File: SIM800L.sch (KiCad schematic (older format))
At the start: 7 parts

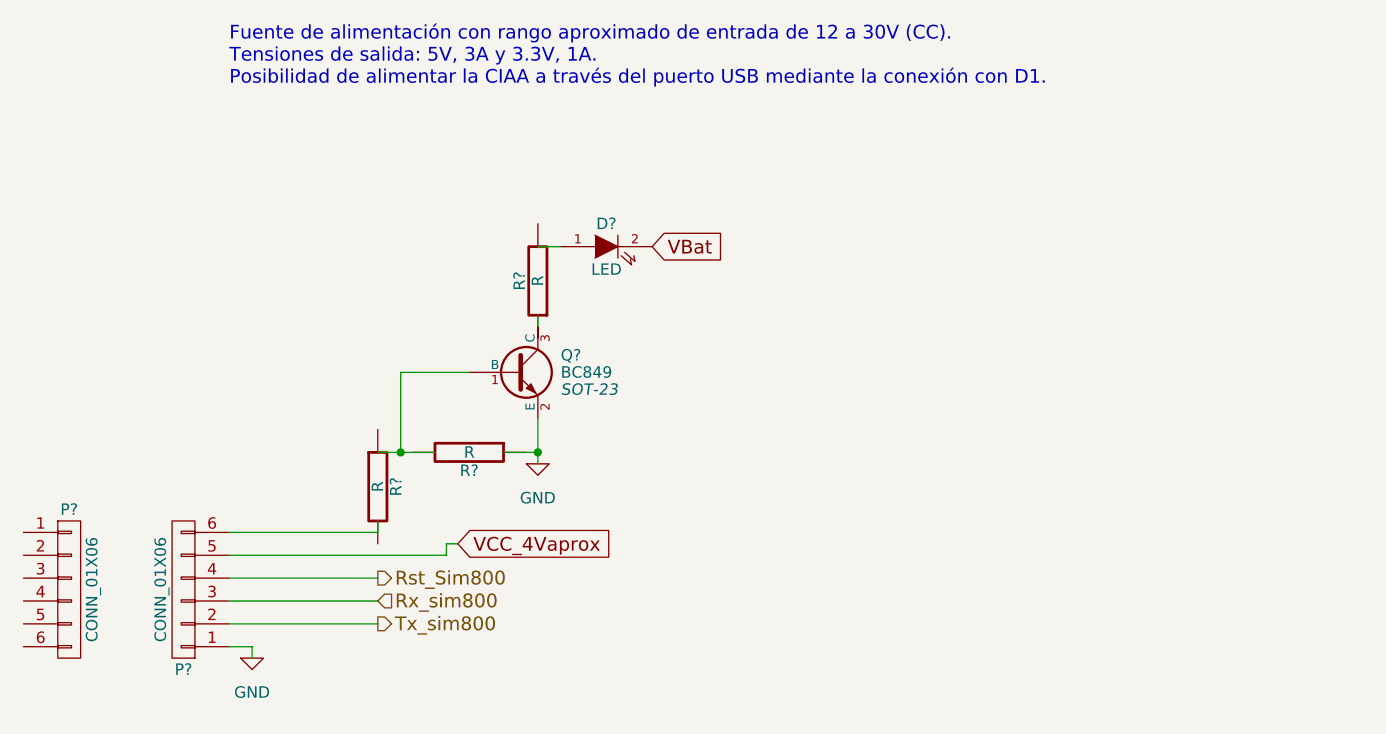
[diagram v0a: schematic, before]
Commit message: Max3232 -ok, Fuente ok, Buttons y Leds, OK. Fuente correinte OK, Falta Potenciometros y LM35.
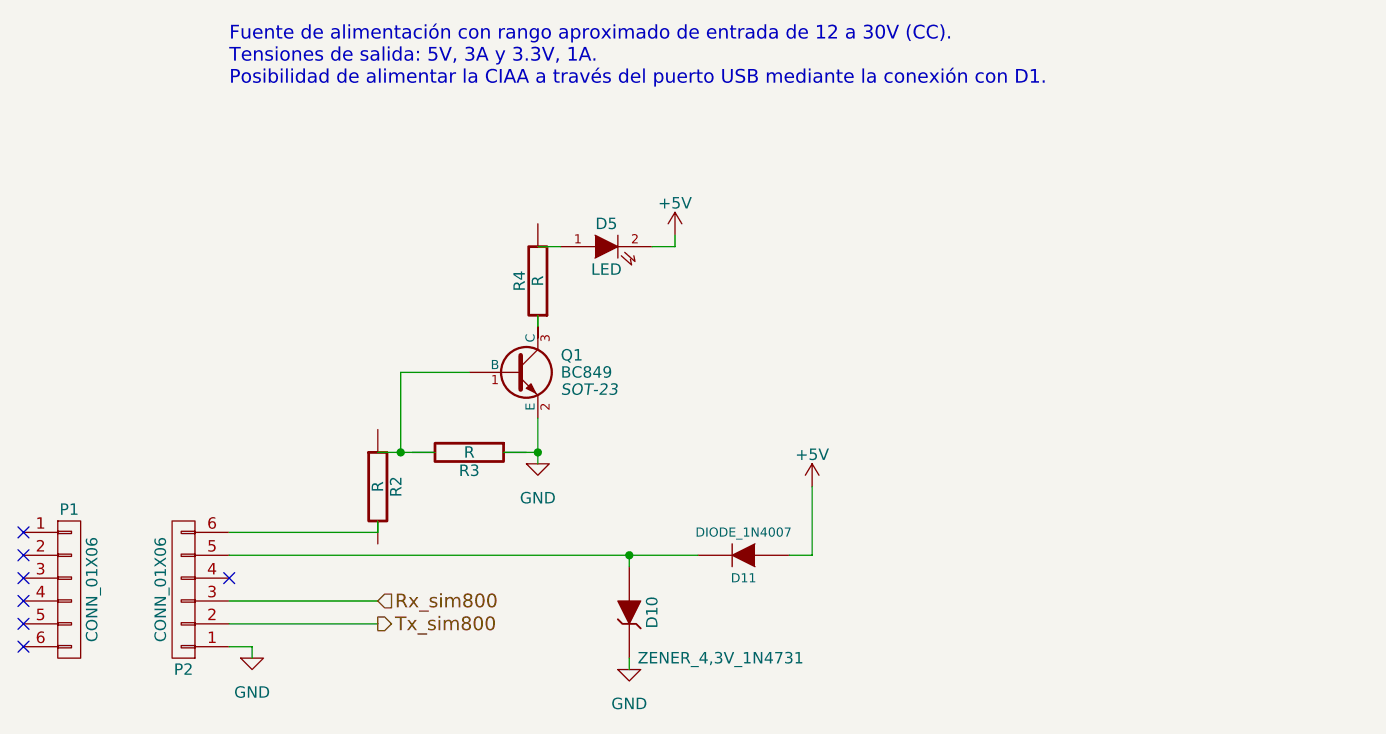
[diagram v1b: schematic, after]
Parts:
- added D10: ZENER_4,3V_1N4731, symbol ZENER
- added D11: DIODE_1N4007, symbol DIODE
- gave numbers to parts that had none: 7
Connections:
- net labels added: +5V
- net labels removed: Rst_Sim800, VBat, VCC_4Vaprox
- wire segments 17 -> 20
- no-connect marks 0 -> 7
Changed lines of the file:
@@
 $Descr A4 11693 8268
 encoding utf-8
-Sheet 4 4
+Sheet 4 6
 Title "CIAA Fuente de alimentación"
 Date "11 may 2015"
@@
 Fuente de alimentación con rango aproximado de entrada de 12 a 30V (CC).\nTensiones de salida: 5V, 3A y 3.3V, 1A.\nPosibilidad de alimentar la CIAA a través del puerto USB mediante la conexión con D1.
 $Comp
-L CONN_01X06 P?
+L CONN_01X06 P1
 U 1 1 5819E820
 P 3350 3450
-F 0 "P?" H 3350 3800 50  0000 C CNN
+F 0 "P1" H 3350 3800 50  0000 C CNN
 F 1 "CONN_01X06" V 3450 3450 50  0000 C CNN
 F 2 "" H 3350 3450 50  0000 C CNN
@@
 $EndComp
 $Comp
-L CONN_01X06 P?
+L CONN_01X06 P2
 U 1 1 5819E8C4
 P 3850 3450
-F 0 "P?" H 3850 3800 50  0000 C CNN
+F 0 "P2" H 3850 3800 50  0000 C CNN
 F 1 "CONN_01X06" V 3950 3450 50  0000 C CNN
 F 2 "" H 3850 3450 50  0000 C CNN
@@
 $EndComp
 $Comp
-L GND #PWR?
+L GND #PWR029
 U 1 1 5819E9A3
 P 4150 3750
-F 0 "#PWR?" H 4150 3500 50  0001 C CNN
+F 0 "#PWR029" H 4150 3500 50  0001 C CNN
 F 1 "GND" H 4150 3600 50  0000 C CNN
 F 2 "" H 4150 3750 50  0000 C CNN
@@
 	4050 3500 4700 3500
 Wire Wire Line
-	4050 3400 4700 3400
-Wire Wire Line
-	4050 3300 5000 3300
+	4050 3300 6100 3300
 Wire Wire Line
 	4050 3200 4700 3200
@@
 Text HLabel 4700 3600 2    60   Output ~ 0
 Tx_sim800
-Text HLabel 4700 3400 2    60   Output ~ 0
-Rst_Sim800
-$Comp
-L R R?
+$Comp
+L R R2
 U 1 1 5819EB4E
 P 4700 3000
-F 0 "R?" V 4780 3000 50  0000 C CNN
+F 0 "R2" V 4780 3000 50  0000 C CNN
 F 1 "R" V 4700 3000 50  0000 C CNN
 F 2 "" V 4630 3000 50  0000 C CNN
@@
 $EndComp
 $Comp
-L R R?
+L R R3
 U 1 1 5819EB9D
 P 5100 2850
-F 0 "R?" V 5180 2850 50  0000 C CNN
+F 0 "R3" V 5180 2850 50  0000 C CNN
 F 1 "R" V 5100 2850 50  0000 C CNN
 F 2 "" V 5030 2850 50  0000 C CNN
@@
 $EndComp
 $Comp
-L BC849 Q?
+L BC849 Q1
 U 1 1 5819ECA4
 P 5300 2500
-F 0 "Q?" H 5500 2575 50  0000 L CNN
+F 0 "Q1" H 5500 2575 50  0000 L CNN
 F 1 "BC849" H 5500 2500 50  0000 L CNN
 F 2 "SOT-23" H 5500 2425 50  0000 L CIN
@@
 $EndComp
 $Comp
-L GND #PWR?
+L GND #PWR030
 U 1 1 5819EDBF
 P 5400 2900
-F 0 "#PWR?" H 5400 2650 50  0001 C CNN
+F 0 "#PWR030" H 5400 2650 50  0001 C CNN
 F 1 "GND" H 5400 2750 50  0000 C CNN
 F 2 "" H 5400 2900 50  0000 C CNN
@@
 Connection ~ 4800 2850
 $Comp
-L R R?
+L R R4
 U 1 1 5819EF54
 P 5400 2100
-F 0 "R?" V 5480 2100 50  0000 C CNN
+F 0 "R4" V 5480 2100 50  0000 C CNN
 F 1 "R" V 5400 2100 50  0000 C CNN
 F 2 "" V 5330 2100 50  0000 C CNN
@@
 $EndComp
 $Comp
-L LED D?
+L LED D5
 U 1 1 5819EFAC
 P 5700 1950
-F 0 "D?" H 5700 2050 50  0000 C CNN
+F 0 "D5" H 5700 2050 50  0000 C CNN
 F 1 "LED" H 5700 1850 50  0000 C CNN
 F 2 "" H 5700 1950 50  0000 C CNN
@@
 Wire Wire Line
 	5400 2250 5400 2300
-Text GLabel 5050 3250 2    60   Input ~ 0
-VCC_4Vaprox
-Wire Wire Line
-	5050 3250 5000 3250
-Wire Wire Line
-	5000 3250 5000 3300
-Text GLabel 5900 1950 2    60   Input ~ 0
-VBat
+NoConn ~ 3150 3700
+NoConn ~ 3150 3600
+NoConn ~ 3150 3500
+NoConn ~ 3150 3400
+NoConn ~ 3150 3300
+NoConn ~ 3150 3200
+$Comp
+L +5V #PWR031
+U 1 1 5819C8CC
+P 6000 1900
+F 0 "#PWR031" H 6000 1750 50  0001 C CNN
+F 1 "+5V" H 6000 2040 50  0000 C CNN
+F 2 "" H 6000 1900 50  0000 C CNN
+F 3 "" H 6000 1900 50  0000 C CNN
+	1    6000 1900
+	1    0    0    -1
+$EndComp
+Wire Wire Line
+	5900 1950 6000 1950
+Wire Wire Line
+	6000 1950 6000 1900
+$Comp
+L ZENER D10
+U 1 1 5819CB42
+P 5800 3550
+F 0 "D10" H 5800 3650 50  0000 C CNN
+F 1 "ZENER_4,3V_1N4731" V 6000 3950 50  0000 C CNN
+F 2 "" H 5800 3550 50  0000 C CNN
+F 3 "" H 5800 3550 50  0000 C CNN
+	1    5800 3550
+	0    1    1    0
+$EndComp
+Wire Wire Line
+	5800 3300 5800 3350
+$Comp
+L GND #PWR032
+U 1 1 5819CBD8
+P 5800 3800
+F 0 "#PWR032" H 5800 3550 50  0001 C CNN
+F 1 "GND" H 5800 3650 50  0000 C CNN
+F 2 "" H 5800 3800 50  0000 C CNN
+F 3 "" H 5800 3800 50  0000 C CNN
+	1    5800 3800
+	1    0    0    -1
+$EndComp
+Wire Wire Line
+	5800 3750 5800 3800
+$Comp
+L DIODE D11
+U 1 1 5819CC13
+P 6300 3300
+F 0 "D11" H 6300 3400 40  0000 C CNN
+F 1 "DIODE_1N4007" H 6300 3200 40  0000 C CNN
+F 2 "" H 6300 3300 60  0000 C CNN
+F 3 "" H 6300 3300 60  0000 C CNN
+	1    6300 3300
+	-1   0    0    1
+$EndComp
+$Comp
+L +5V #PWR033
+U 1 1 5819CCE8
+P 6600 3000
+F 0 "#PWR033" H 6600 2850 50  0001 C CNN
+F 1 "+5V" H 6600 3140 50  0000 C CNN
+F 2 "" H 6600 3000 50  0000 C CNN
+F 3 "" H 6600 3000 50  0000 C CNN
+	1    6600 3000
+	1    0    0    -1
+$EndComp
+Wire Wire Line
+	6600 3000 6600 3300
+Wire Wire Line
+	6600 3300 6500 3300
+Connection ~ 5800 3300
+NoConn ~ 4050 3400
 $EndSCHEMATC

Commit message: Arreglo Max3232_ok, Fuente_ok, Buttons&Leds, OK.Fuente correinte OK, Potenciometros OK y LM35 OK.
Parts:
- removed P1: CONN_01X06, symbol CONN_01X06
- added P3: CONN_01X06, symbol CONN_01X06
- renumbered D10 to D6, D11 to D7, P2 to P4
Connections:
- wire segments 20 -> 21
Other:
- moved on the sheet: D5, Q1, R2, R3, R4
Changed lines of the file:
@@
 EESchema Schematic File Version 2
-LIBS:ciaa-nxp-rescue
-LIBS:power
-LIBS:device
-LIBS:transistors
-LIBS:conn
-LIBS:linear
-LIBS:regul
-LIBS:74xx
-LIBS:cmos4000
-LIBS:adc-dac
-LIBS:memory
-LIBS:xilinx
-LIBS:microcontrollers
-LIBS:dsp
-LIBS:microchip
-LIBS:analog_switches
-LIBS:motorola
-LIBS:texas
-LIBS:intel
-LIBS:audio
-LIBS:interface
-LIBS:digital-audio
-LIBS:philips
-LIBS:display
-LIBS:cypress
-LIBS:siliconi
-LIBS:opto
-LIBS:atmel
-LIBS:contrib
-LIBS:valves
+LIBS:sensors
 LIBS:74LVC1G04GW
+LIBS:93CXX
+LIBS:BLM15HG6015N1D
+LIBS:FT2232H
+LIBS:IS42S16400F
+LIBS:LPC4337JBD144
+LIBS:MIC2025
+LIBS:PBSS5240
+LIBS:PRTR5V0U2X
+LIBS:PS2805
+LIBS:SCHA5B0200
+LIBS:Si50x
+LIBS:TJA1040
+LIBS:TXB0108
+LIBS:Transil_diode
 LIBS:amesser-ad
 LIBS:amesser-cmos4000
@@
 LIBS:audio-vlsi
 LIBS:bat54_c
-LIBS:BLM15HG6015N1D
+LIBS:capteurs
+LIBS:fqt13n06l
 LIBS:g5v2
 LIBS:lm2596
+LIBS:mcp1415
+LIBS:mcp1416
 LIBS:mcu-nxp
 LIBS:mcu-st
-LIBS:MIC2025
+LIBS:my_lab
 LIBS:net-phy
 LIBS:nsi50010yt1g
-LIBS:PRTR5V0U2X
+LIBS:pbss5240xf
 LIBS:regulators
 LIBS:rs485_rs232_can
 LIBS:s25fl032p0xmfi013
-LIBS:SCHA5B0200
-LIBS:Si50x
-LIBS:Transil_diode
+LIBS:sw_push
+LIBS:tvs
 LIBS:w_device
-LIBS:LPC4337JBD144
-LIBS:IS42S16400F
-LIBS:TXB0108
-LIBS:FT2232H
-LIBS:93CXX
-LIBS:TJA1040
-LIBS:tvs
-LIBS:PBSS5240
-LIBS:pbss5240xf
-LIBS:sw_push
-LIBS:mcp1416
-LIBS:fqt13n06l
+LIBS:74xgxx
+LIBS:74xx
+LIBS:Altera
+LIBS:ESD_Protection
+LIBS:Lattice
+LIBS:Oscillators
+LIBS:Power_Management
+LIBS:Worldsemi
+LIBS:Xicor
+LIBS:Zilog
+LIBS:ac-dc
+LIBS:actel
+LIBS:adc-dac
+LIBS:analog_devices
+LIBS:analog_switches
+LIBS:atmel
+LIBS:audio
+LIBS:brooktre
+LIBS:cmos4000
+LIBS:cmos_ieee
+LIBS:conn
+LIBS:contrib
+LIBS:cypress
+LIBS:dc-dc
+LIBS:device
+LIBS:digital-audio
+LIBS:diode
+LIBS:display
+LIBS:dsp
+LIBS:elec-unifil
+LIBS:ftdi
+LIBS:gennum
+LIBS:graphic
+LIBS:hc11
+LIBS:intel
+LIBS:interface
+LIBS:ir
+LIBS:linear
+LIBS:logo
+LIBS:maxim
+LIBS:memory
+LIBS:microchip
+LIBS:microchip_dspic33dsc
+LIBS:microchip_pic10mcu
+LIBS:microchip_pic12mcu
+LIBS:microchip_pic16mcu
+LIBS:microchip_pic18mcu
+LIBS:microchip_pic32mcu
+LIBS:microcontrollers
+LIBS:motor_drivers
+LIBS:motorola
+LIBS:msp430
+LIBS:nordicsemi
+LIBS:nxp_armmcu
+LIBS:onsemi
+LIBS:opto
+LIBS:philips
+LIBS:power
+LIBS:powerint
+LIBS:pspice
+LIBS:references
+LIBS:regul
+LIBS:relays
+LIBS:rfcom
+LIBS:silabs
+LIBS:siliconi
+LIBS:stm8
+LIBS:stm32
+LIBS:supertex
+LIBS:switches
+LIBS:texas
+LIBS:transf
+LIBS:transistors
+LIBS:ttl_ieee
+LIBS:valves
+LIBS:video
+LIBS:xilinx
 LIBS:ciaa-nxp-cache
 EELAYER 25 0
@@
 Fuente de alimentación con rango aproximado de entrada de 12 a 30V (CC).\nTensiones de salida: 5V, 3A y 3.3V, 1A.\nPosibilidad de alimentar la CIAA a través del puerto USB mediante la conexión con D1.
 $Comp
-L CONN_01X06 P1
-U 1 1 5819E820
+L CONN_01X06 P3
+U 1 1 5819FDA4
 P 3350 3450
-F 0 "P1" H 3350 3800 50  0000 C CNN
+F 0 "P3" H 3350 3800 50  0000 C CNN
 F 1 "CONN_01X06" V 3450 3450 50  0000 C CNN
 F 2 "" H 3350 3450 50  0000 C CNN
@@
 $EndComp
 $Comp
-L CONN_01X06 P2
+L CONN_01X06 P4
 U 1 1 5819E8C4
 P 3850 3450
-F 0 "P2" H 3850 3800 50  0000 C CNN
+F 0 "P4" H 3850 3800 50  0000 C CNN
 F 1 "CONN_01X06" V 3950 3450 50  0000 C CNN
 F 2 "" H 3850 3450 50  0000 C CNN
@@
 Wire Wire Line
 	4050 3300 6100 3300
-Wire Wire Line
-	4050 3200 4700 3200
 Text HLabel 4700 3500 2    60   Input ~ 0
 Rx_sim800
@@
 L R R2
 U 1 1 5819EB4E
-P 4700 3000
-F 0 "R2" V 4780 3000 50  0000 C CNN
-F 1 "R" V 4700 3000 50  0000 C CNN
-F 2 "" V 4630 3000 50  0000 C CNN
-F 3 "" H 4700 3000 50  0000 C CNN
-	1    4700 3000
+P 4450 2750
+F 0 "R2" V 4530 2750 50  0000 C CNN
+F 1 "R" V 4450 2750 50  0000 C CNN
+F 2 "" V 4380 2750 50  0000 C CNN
+F 3 "" H 4450 2750 50  0000 C CNN
+	1    4450 2750
 	1    0    0    -1
 $EndComp
@@
 L R R3
 U 1 1 5819EB9D
-P 5100 2850
-F 0 "R3" V 5180 2850 50  0000 C CNN
-F 1 "R" V 5100 2850 50  0000 C CNN
-F 2 "" V 5030 2850 50  0000 C CNN
-F 3 "" H 5100 2850 50  0000 C CNN
-	1    5100 2850
+P 5100 2750
+F 0 "R3" V 5180 2750 50  0000 C CNN
+F 1 "R" V 5100 2750 50  0000 C CNN
+F 2 "" V 5030 2750 50  0000 C CNN
+F 3 "" H 5100 2750 50  0000 C CNN
+	1    5100 2750
 	0    1    1    0
 $EndComp
@@
 L BC849 Q1
 U 1 1 5819ECA4
-P 5300 2500
-F 0 "Q1" H 5500 2575 50  0000 L CNN
-F 1 "BC849" H 5500 2500 50  0000 L CNN
-F 2 "SOT-23" H 5500 2425 50  0000 L CIN
-F 3 "" H 5300 2500 50  0000 L CNN
-	1    5300 2500
+P 5300 2400
+F 0 "Q1" H 5500 2475 50  0000 L CNN
+F 1 "BC849" H 5500 2400 50  0000 L CNN
+F 2 "SOT-23" H 5500 2325 50  0000 L CIN
+F 3 "" H 5300 2400 50  0000 L CNN
+	1    5300 2400
 	1    0    0    -1
 $EndComp
@@
 L GND #PWR030
 U 1 1 5819EDBF
-P 5400 2900
-F 0 "#PWR030" H 5400 2650 50  0001 C CNN
-F 1 "GND" H 5400 2750 50  0000 C CNN
-F 2 "" H 5400 2900 50  0000 C CNN
-F 3 "" H 5400 2900 50  0000 C CNN
-	1    5400 2900
-	1    0    0    -1
-$EndComp
-Wire Wire Line
-	5400 2700 5400 2900
-Wire Wire Line
-	5250 2850 5400 2850
-Connection ~ 5400 2850
-Wire Wire Line
-	4700 2850 4950 2850
-Wire Wire Line
-	4700 3200 4700 3150
-Wire Wire Line
-	5100 2500 4800 2500
-Wire Wire Line
-	4800 2500 4800 2850
-Connection ~ 4800 2850
+P 5400 2800
+F 0 "#PWR030" H 5400 2550 50  0001 C CNN
+F 1 "GND" H 5400 2650 50  0000 C CNN
+F 2 "" H 5400 2800 50  0000 C CNN
+F 3 "" H 5400 2800 50  0000 C CNN
+	1    5400 2800
+	1    0    0    -1
+$EndComp
+Wire Wire Line
+	5400 2600 5400 2800
+Connection ~ 5400 2750
+Wire Wire Line
+	4450 2400 5100 2400
 $Comp
 L R R4
 U 1 1 5819EF54
-P 5400 2100
-F 0 "R4" V 5480 2100 50  0000 C CNN
-F 1 "R" V 5400 2100 50  0000 C CNN
-F 2 "" V 5330 2100 50  0000 C CNN
-F 3 "" H 5400 2100 50  0000 C CNN
-	1    5400 2100
+P 5400 1800
+F 0 "R4" V 5480 1800 50  0000 C CNN
+F 1 "R" V 5400 1800 50  0000 C CNN
+F 2 "" V 5330 1800 50  0000 C CNN
+F 3 "" H 5400 1800 50  0000 C CNN
+	1    5400 1800
 	-1   0    0    1
 $EndComp
@@
 L LED D5
 U 1 1 5819EFAC
-P 5700 1950
-F 0 "D5" H 5700 2050 50  0000 C CNN
-F 1 "LED" H 5700 1850 50  0000 C CNN
-F 2 "" H 5700 1950 50  0000 C CNN
-F 3 "" H 5700 1950 50  0000 C CNN
-	1    5700 1950
-	1    0    0    -1
-$EndComp
-Wire Wire Line
-	5400 1950 5500 1950
-Wire Wire Line
-	5400 2250 5400 2300
+P 5700 1550
+F 0 "D5" H 5700 1650 50  0000 C CNN
+F 1 "LED" H 5700 1450 50  0000 C CNN
+F 2 "" H 5700 1550 50  0000 C CNN
+F 3 "" H 5700 1550 50  0000 C CNN
+	1    5700 1550
+	1    0    0    -1
+$EndComp
+Wire Wire Line
+	5400 2050 5400 2200
 NoConn ~ 3150 3700
 NoConn ~ 3150 3600
@@
 L +5V #PWR031
 U 1 1 5819C8CC
-P 6000 1900
-F 0 "#PWR031" H 6000 1750 50  0001 C CNN
-F 1 "+5V" H 6000 2040 50  0000 C CNN
-F 2 "" H 6000 1900 50  0000 C CNN
-F 3 "" H 6000 1900 50  0000 C CNN
-	1    6000 1900
-	1    0    0    -1
-$EndComp
-Wire Wire Line
-	5900 1950 6000 1950
-Wire Wire Line
-	6000 1950 6000 1900
-$Comp
-L ZENER D10
+P 6000 1500
+F 0 "#PWR031" H 6000 1350 50  0001 C CNN
+F 1 "+5V" H 6000 1640 50  0000 C CNN
+F 2 "" H 6000 1500 50  0000 C CNN
+F 3 "" H 6000 1500 50  0000 C CNN
+	1    6000 1500
+	1    0    0    -1
+$EndComp
+Wire Wire Line
+	5900 1550 6000 1550
+Wire Wire Line
+	6000 1550 6000 1500
+$Comp
+L ZENER D6
 U 1 1 5819CB42
 P 5800 3550
-F 0 "D10" H 5800 3650 50  0000 C CNN
+F 0 "D6" H 5800 3650 50  0000 C CNN
 F 1 "ZENER_4,3V_1N4731" V 6000 3950 50  0000 C CNN
 F 2 "" H 5800 3550 50  0000 C CNN
@@
 	5800 3750 5800 3800
 $Comp
-L DIODE D11
+L DIODE D7
 U 1 1 5819CC13
 P 6300 3300
-F 0 "D11" H 6300 3400 40  0000 C CNN
+F 0 "D7" H 6300 3400 40  0000 C CNN
 F 1 "DIODE_1N4007" H 6300 3200 40  0000 C CNN
 F 2 "" H 6300 3300 60  0000 C CNN
@@
 Connection ~ 5800 3300
 NoConn ~ 4050 3400
+Wire Wire Line
+	4050 3200 4450 3200
+Wire Wire Line
+	4450 3200 4450 3000
+Wire Wire Line
+	4450 2500 4450 2400
+Wire Wire Line
+	4850 2750 4750 2750
+Wire Wire Line
+	4750 2750 4750 2400
+Connection ~ 4750 2400
+Wire Wire Line
+	5350 2750 5400 2750
+Wire Wire Line
+	5500 1550 5400 1550
 $EndSCHEMATC
